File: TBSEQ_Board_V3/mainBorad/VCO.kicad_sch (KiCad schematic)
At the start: 29 parts, among them IC5 NJM2125F-TE1, J13 Conn_01x01_Pin, Q24 NPN, Q25 NPN, Q26 HN1C01FU-GR,LF, Q27 PNP, Q28 NJFET, Q8 PNP, SW1 2MS1T1B4VS2QES

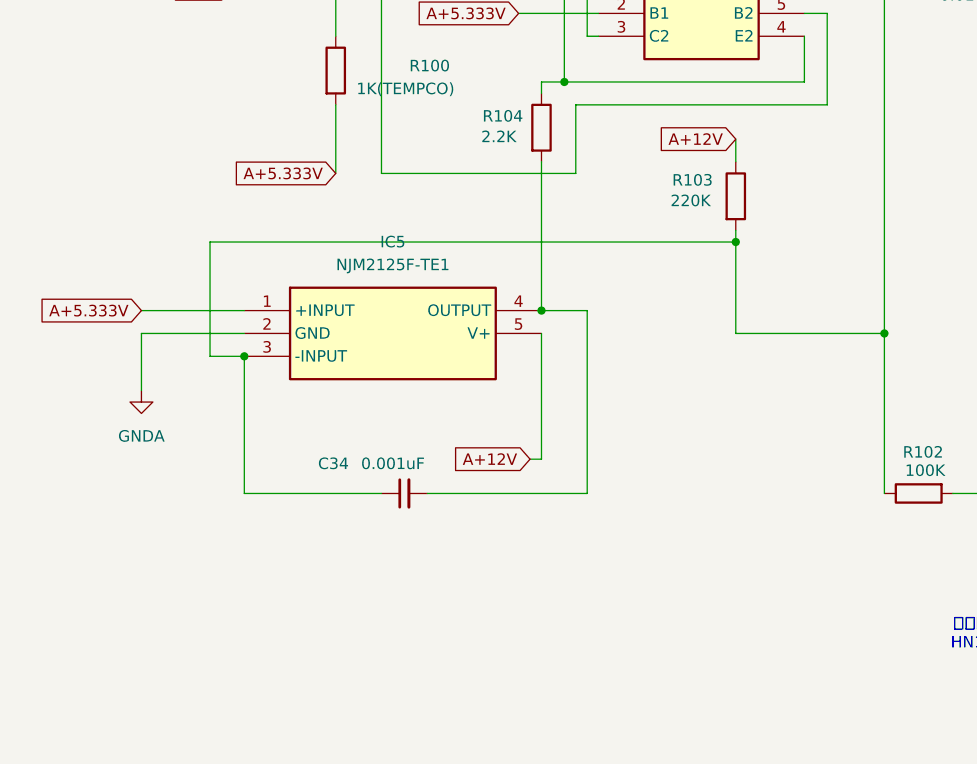
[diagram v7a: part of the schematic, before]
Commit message: V3Board
DualTr OPAmp やはりDIPに変更してオートルーター前に戻す
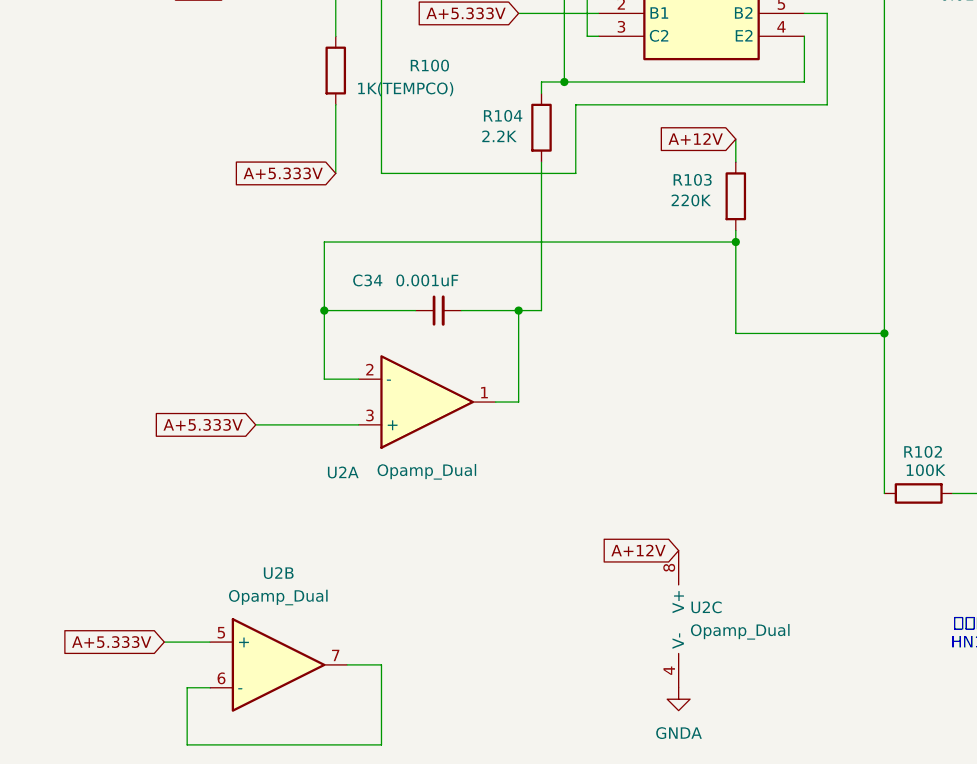
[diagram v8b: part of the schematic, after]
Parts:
- removed IC5: NJM2125F-TE1, SamacSys_Parts:SOT95P280X130-5N, symbol SamacSys_Parts:NJM2125F-TE1
- added U2: Opamp_Dual, Package_DIP:DIP-8_W7.62mm_Socket_LongPads, symbol Device:Opamp_Dual
- Q26: footprint SamacSys_Parts:HN1C01FUGRLF -> SamacSys_Parts:HN1C01FUGRLF_DIP8
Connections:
- net A+12V: now also U2.8 (V+)
- net A+5.333V: now also U2.3 (+), U2.5 (+)
- net GNDA: now also U2.4 (V-)
- net at C34.1, Q26.6 (C1), R102.1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: now also U2.2 (-)
- net at C34.2, R104.2: now also U2.1
- new net: U2.6 (-), U2.7
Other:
- moved on the sheet: C34
